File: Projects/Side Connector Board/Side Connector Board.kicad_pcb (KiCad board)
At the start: 2 copper layers, 165.2 x 35.1 mm, 18 parts, among them P10 CONN_02X04, P2 CONN_02X04, P4 CONN_02X04, P6 CONN_02X04, P8 CONN_02X04

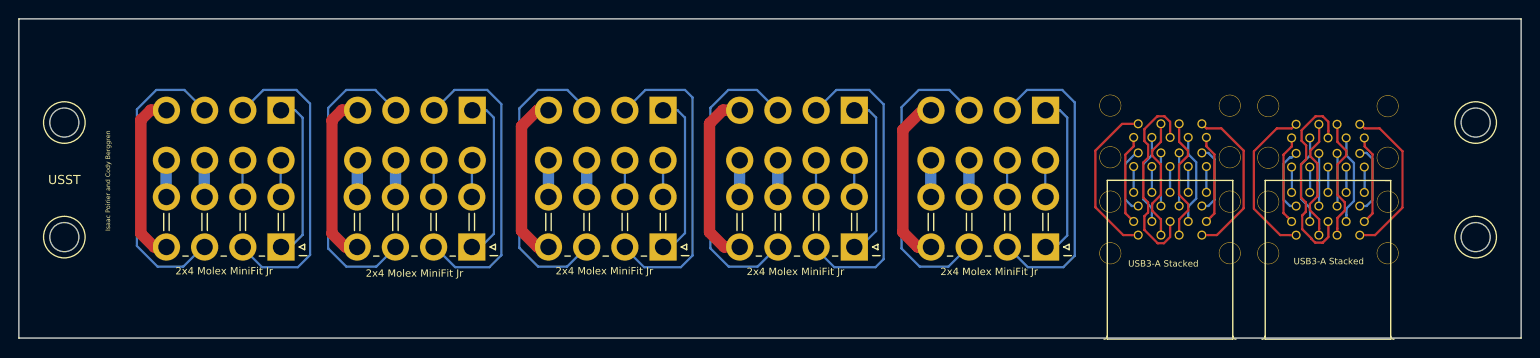
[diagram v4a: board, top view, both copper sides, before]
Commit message: finished refactor of pcb panels for Electrical Tray. Ready for ordering
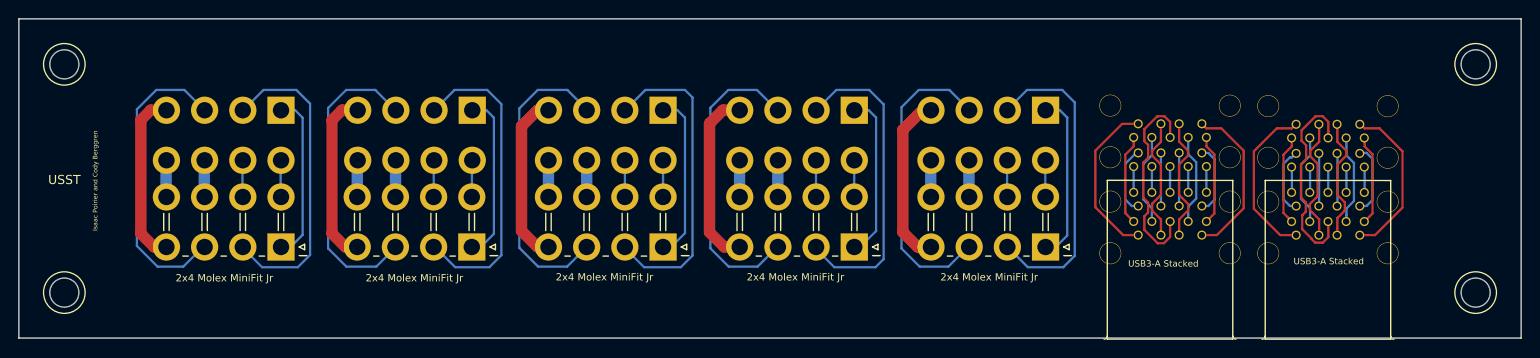
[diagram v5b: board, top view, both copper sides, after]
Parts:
- 2x4 Molex MiniFit Jr: renamed from P10
- 2x4 Molex MiniFit Jr: renamed from P2
- 2x4 Molex MiniFit Jr: renamed from P4
- 2x4 Molex MiniFit Jr: renamed from P6
- 2x4 Molex MiniFit Jr: renamed from P8
- moved REF** 6.40 mm to (225.2, 90.2)
- moved REF** 6.40 mm to (70.0, 90.2)
- moved REF** 6.10 mm to (70.0, 115.3)
- moved REF** 6.10 mm to (225.2, 115.3)
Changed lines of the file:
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@@
     (links 76)
     (no_connects 0)
-    (area 64.924999 91.524999 230.275001 114.275001)
+    (area 64.924999 80.674999 230.275001 124.861801)
     (thickness 1.6)
-    (drawings 6)
+    (drawings 10)
     (tracks 351)
     (zones 0)
@@
   )
   (module Connect:1pin (layer F.Cu)
-    (at 225.2 96.6)
+    (at 225.2 90.2)
     (descr "module 1 pin (ou trou mecanique de percage)")
     (tags DEV)
@@
   )
   (module Connect:1pin (layer F.Cu)
-    (at 70 96.6)
+    (at 70 90.2)
     (descr "module 1 pin (ou trou mecanique de percage)")
     (tags DEV)
@@
   )
   (module Connect:1pin (layer F.Cu)
-    (at 70 109.2)
+    (at 70 115.3)
     (descr "module 1 pin (ou trou mecanique de percage)")
     (tags DEV)
@@
   )
   (module Connect:1pin (layer F.Cu)
-    (at 225.2 109.2)
+    (at 225.2 115.3)
     (descr "module 1 pin (ou trou mecanique de percage)")
     (tags DEV)
@@
     (descr "Molex Mini-Fit JR, PN:5569-08A2, dual row, side entry type, through hole, with plastic peg mount")
     (tags "connector molex mini-fit 5569")
-    (fp_text reference "2x4 Molex MiniFit Jr" (at 6.2484 -2.6416 180) (layer F.SilkS)
+    (fp_text reference "2x4 Molex MiniFit Jr" (at 6.2276 -3.4132 180) (layer F.SilkS)
       (effects (font (size 0.8 0.8) (thickness 0.15)))
     )
@@
     (descr "Molex Mini-Fit JR, PN:5569-08A2, dual row, side entry type, through hole, with plastic peg mount")
     (tags "connector molex mini-fit 5569")
-    (fp_text reference P2 (at 6.5276 2.55 180) (layer B.SilkS)
+    (fp_text reference "2x4 Molex MiniFit Jr" (at 6.5276 3.25 180) (layer B.SilkS)
       (effects (font (size 1 1) (thickness 0.15)) (justify mirror))
     )
@@
     (descr "Molex Mini-Fit JR, PN:5569-08A2, dual row, side entry type, through hole, with plastic peg mount")
     (tags "connector molex mini-fit 5569")
-    (fp_text reference "2x4 Molex MiniFit Jr" (at 6.2992 -2.8956 180) (layer F.SilkS)
+    (fp_text reference "2x4 Molex MiniFit Jr" (at 6.308 -3.4132 180) (layer F.SilkS)
       (effects (font (size 0.8 0.8) (thickness 0.15)))
     )
@@
     (descr "Molex Mini-Fit JR, PN:5569-08A2, dual row, side entry type, through hole, with plastic peg mount")
     (tags "connector molex mini-fit 5569")
-    (fp_text reference P4 (at 6.2992 2.6416 180) (layer B.SilkS)
+    (fp_text reference "2x4 Molex MiniFit Jr" (at 6.3588 3.25 180) (layer B.SilkS)
       (effects (font (size 1 1) (thickness 0.15)) (justify mirror))
     )
@@
     (descr "Molex Mini-Fit JR, PN:5569-08A2, dual row, side entry type, through hole, with plastic peg mount")
     (tags "connector molex mini-fit 5569")
-    (fp_text reference "2x4 Molex MiniFit Jr" (at 6.4516 -2.6416 180) (layer F.SilkS)
+    (fp_text reference "2x4 Molex MiniFit Jr" (at 6.4392 -3.3132 180) (layer F.SilkS)
       (effects (font (size 0.8 0.8) (thickness 0.15)))
     )
@@
     (descr "Molex Mini-Fit JR, PN:5569-08A2, dual row, side entry type, through hole, with plastic peg mount")
     (tags "connector molex mini-fit 5569")
-    (fp_text reference P6 (at 6.3392 2.45 180) (layer B.SilkS)
+    (fp_text reference "2x4 Molex MiniFit Jr" (at 6.3392 3.25 180) (layer B.SilkS)
       (effects (font (size 1 1) (thickness 0.15)) (justify mirror))
     )
@@
     (descr "Molex Mini-Fit JR, PN:5569-08A2, dual row, side entry type, through hole, with plastic peg mount")
     (tags "connector molex mini-fit 5569")
-    (fp_text reference "2x4 Molex MiniFit Jr" (at 6.4704 -2.7132 180) (layer F.SilkS)
+    (fp_text reference "2x4 Molex MiniFit Jr" (at 6.4704 -3.3132 180) (layer F.SilkS)
       (effects (font (size 0.8 0.8) (thickness 0.15)))
     )
@@
     (descr "Molex Mini-Fit JR, PN:5569-08A2, dual row, side entry type, through hole, with plastic peg mount")
     (tags "connector molex mini-fit 5569")
-    (fp_text reference P8 (at 6.6548 2.65 180) (layer B.SilkS)
+    (fp_text reference "2x4 Molex MiniFit Jr" (at 6.6548 3.25 180) (layer B.SilkS)
       (effects (font (size 1 1) (thickness 0.15)) (justify mirror))
     )
@@
     (descr "Molex Mini-Fit JR, PN:5569-08A2, dual row, side entry type, through hole, with plastic peg mount")
     (tags "connector molex mini-fit 5569")
-    (fp_text reference "2x4 Molex MiniFit Jr" (at 6.2016 -2.7132 180) (layer F.SilkS)
+    (fp_text reference "2x4 Molex MiniFit Jr" (at 6.2016 -3.3132 180) (layer F.SilkS)
       (effects (font (size 0.8 0.8) (thickness 0.15)))
     )
@@
     (descr "Molex Mini-Fit JR, PN:5569-08A2, dual row, side entry type, through hole, with plastic peg mount")
     (tags "connector molex mini-fit 5569")
-    (fp_text reference P10 (at 6.4008 2.55 180) (layer B.SilkS)
+    (fp_text reference "2x4 Molex MiniFit Jr" (at 6.4016 3.25 180) (layer B.SilkS)
       (effects (font (size 1 1) (thickness 0.15)) (justify mirror))
     )
@@
     )
   )
+  (gr_line (start 220.2 88.2) (end 75 88.2) (layer Dwgs.User) (width 0.2))
+  (gr_line (start 220.2 117.3) (end 220.2 88.2) (layer Dwgs.User) (width 0.2))
+  (gr_line (start 75 117.3) (end 220.2 117.3) (layer Dwgs.User) (width 0.2))
+  (gr_line (start 75 88.2) (end 75 117.3) (layer Dwgs.User) (width 0.2))
   (gr_text USST (at 70 102.9) (layer F.SilkS)
     (effects (font (size 1 1) (thickness 0.25)))
@@
   (gr_line (start 65 120.3) (end 230.2 120.3) (angle 90) (layer Edge.Cuts) (width 0.15))
   (gr_line (start 65 85.2) (end 65 120.3) (angle 90) (layer Edge.Cuts) (width 0.15))
-  (gr_text "Isaac Poirier and Cody Berggren" (at 74.8 103 90) (layer F.SilkS)
+  (gr_text "Isaac Poirier and Cody Berggren" (at 73.4 103 90) (layer F.SilkS)
     (effects (font (size 0.5 0.5) (thickness 0.125)))
   )
